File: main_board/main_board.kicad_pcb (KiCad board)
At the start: 2 copper layers, 160 x 110 mm, 154 parts, among them IC1 MP2722GRH-0000-Z, IC2 MP3429GL-Z, IC3 NX3DV42GU, IC4 TS921ID, IC5 CY7C65632-28LTXC, IC6 TS921ID, J1 USB3_A, J10 Conn_01x22_Female, J2 USB3_A, J22 690-019-298-412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

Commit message: Rev 1 draft
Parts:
- removed C18, C9: 100n, Capacitor_SMD:C_0805_2012Metric_Pad1.18x1.45mm_HandSolder
- removed H1, H2, H3, H4, H5, H6, H7, H8: MountingHole, CM5IO:MountingHole_2.7mm_M2.5_DIN965
- removed IC3: NX3DV42GU, 000_custom:NX3DV42GU
- removed the JMP at (113.6, 41.8)
- removed the JMP at (42.5, 37.8)
- added C65: 1u, Capacitor_SMD:C_0805_2012Metric_Pad1.18x1.45mm_HandSolder, F.Cu at (44.8, 36.0)
- added C66: 1u, Capacitor_SMD:C_0805_2012Metric_Pad1.18x1.45mm_HandSolder, F.Cu at (40.5, 35.9)
- added C67: 1u, Capacitor_SMD:C_0805_2012Metric_Pad1.18x1.45mm_HandSolder, F.Cu at (53.8, 31.8)
- added J11: 501568-0607-TR325, 000_custom:CONN_501568-0607-TR325_MOL, F.Cu at (117.6, 76.5)
- added J12: SM04B-XSRS-ETBLFSN, 000_custom:CONN_SM04B-XSRS-ETB_JST, F.Cu at (55.8, 46.7)
- added J13: SM10B-XSRS-ETB, 000_custom:CONN_SM10B-XSRS-ETB_JST, F.Cu at (50.1, 61.4)
- added MOSFET1: STL9P3LLH6, 000_custom:POWERFLAT_3P3X3P3_STM, F.Cu at (52.6, 38.5)
- added U8: STUSB4500QTR, 000_custom:STUSB4500, F.Cu at (42.9, 39.9)
- C1: footprint Capacitor_SMD:C_0805_2012Metric -> Capacitor_SMD:C_0805_2012Metric_Pad1.18x1.45mm_HandSolder
- R23: value 2.2K 1% -> 1K
- R5: value 0R -> 100K
- R9: value 2.2K 1% -> 10K
- moved R23 70.3 mm to (47.8, 37.7), turned to -90 degrees
- moved C15 67.3 mm to (49.0, 125.9), turned to -90 degrees
- moved C14 64.0 mm to (51.0, 125.9), turned to -90 degrees
- moved C4 63.5 mm to (70.8, 126.7), turned to 0 degrees
- moved L1 61.9 mm to (58.8, 124.2)
- moved C6 61.5 mm to (62.9, 125.6)
- moved R3 61.5 mm to (64.9, 125.7)
- moved R4 61.5 mm to (66.9, 125.7)
- moved U1 61.5 mm to (63.3, 122.4)
- moved C1 60.8 mm to (70.8, 124.7), turned to 0 degrees
- moved C10 60.8 mm to (52.8, 125.9), turned to -90 degrees
- moved C5 58.0 mm to (70.8, 122.8), turned to 0 degrees
- moved C11 57.6 mm to (54.7, 125.9), turned to -90 degrees
- moved J2 36.3 mm to (180.7, 110.0)
- moved J6 33.4 mm to (182.4, 76.3)
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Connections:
- C19 pad 1: /Battery management/VIN -> Net-(IC1-IN)
- IC1 pad 1: /Battery management/CC1 -> unconnected-(IC1-CC1-Pad1)
- IC1 pad 2: /Battery management/VIN -> Net-(IC1-IN)
- IC1 pad 20: /Battery management/USBC_MX2_USB2_N -> unconnected-(IC1-D--Pad20)
- IC1 pad 21: /Battery management/USBC_MX2_USB2_P -> unconnected-(IC1-D+-Pad21)
- IC1 pad 22: /Battery management/CC2 -> unconnected-(IC1-CC2_1-Pad22)
- IC1 pad 8: /Battery management/PMIC INTERRUPT -> unconnected-(IC1-~{INT}-Pad8)
- J10 pad 11: /CM5_HighSpeed/DPHY0_D2_N -> /CM5_HighSpeed/DPHY0_D1_P
- J10 pad 12: /CM5_HighSpeed/DPHY0_D2_P -> /CM5_HighSpeed/DPHY0_D1_N
- J10 pad 14: /CM5_HighSpeed/DPHY0_D3_N -> /CM5_HighSpeed/DPHY0_D0_P
- J10 pad 15: /CM5_HighSpeed/DPHY0_D3_P -> /CM5_HighSpeed/DPHY0_D0_N
- J10 pad 17: Net-(J10-Pin_17) -> /CM5_GPIO/+3.3v
- J10 pad 18: unconnected-(J10-Pin_18-Pad18) -> /CM5_GPIO/DPHY1_SDA
- J10 pad 19: GND -> /CM5_GPIO/DPHY1_SCL
- J10 pad 2: /CM5_HighSpeed/DPHY0_D0_N -> /CM5_HighSpeed/DPHY0_D3_P
- J10 pad 20: /CM5_GPIO/DPHY1_SDA -> /Battery management/+5V
- J10 pad 21: /CM5_GPIO/DPHY1_SCL -> /Battery management/+5V
- J10 pad 22: /CM5_GPIO/+3.3v -> /Battery management/+5V
- J10 pad 3: /CM5_HighSpeed/DPHY0_D0_P -> /CM5_HighSpeed/DPHY0_D3_N
- J10 pad 5: /CM5_HighSpeed/DPHY0_D1_N -> /CM5_HighSpeed/DPHY0_D2_P
- J10 pad 6: /CM5_HighSpeed/DPHY0_D1_P -> /CM5_HighSpeed/DPHY0_D2_N
- J10 pad 8: /CM5_HighSpeed/DPHY0_C_N -> /CM5_HighSpeed/DPHY0_C_P
- J10 pad 9: /CM5_HighSpeed/DPHY0_C_P -> /CM5_HighSpeed/DPHY0_C_N
- J2 pad 2: Net-(IC5-DD-[3]) -> Net-(IC5-DD-[1])
- J2 pad 3: Net-(IC5-DD+[3]) -> Net-(IC5-DD+[1])
- J5 pad A4: /Battery management/VIN -> Net-(U8-VDD)
- J5 pad A5: /Battery management/CC1 -> Net-(J5-CC1)
- J5 pad A6: /Battery management/USB2_P -> unconnected-(J5-D+-PadA6)
- J5 pad A7: /Battery management/USB2_N -> unconnected-(J5-D--PadA7)
- J5 pad B4: /Battery management/VIN -> Net-(U8-VDD)
- J5 pad B5: /Battery management/CC2 -> Net-(J5-CC2)
- J5 pad B6: /Battery management/USB2_P -> unconnected-(J5-D+-PadB6)
- J5 pad B7: /Battery management/USB2_N -> unconnected-(J5-D--PadB7)
- J6 pad 2: Net-(IC5-DD+[1]) -> Net-(IC5-DD+[3])
- J6 pad 3: Net-(IC5-DD-[1]) -> Net-(IC5-DD-[3])
- Module1 pad 103: /Battery management/USBC_MX1_USB2_N -> Net-(Module1B-USB2_N)
- Module1 pad 105: /Battery management/USBC_MX1_USB2_P -> Net-(Module1B-USB2_P)
- R12 pad 1: Net-(U6-ILIM) -> GND
- R12 pad 2: GND -> Net-(U6-ILIM)
- R23 pad 1: /CM5_GPIO/+3.3v -> Net-(U8-VDD)
- R23 pad 2: Net-(J10-Pin_17) -> Net-(U8-VBUS_VS_DISCH)
- R5 pad 1: /Battery management/USB2_N -> Net-(U8-VDD)
- R5 pad 2: /Battery management/USB2_N -> Net-(MOSFET1-G)
- R9 pad 1: /Battery management/VIN -> Net-(MOSFET1-G)
- R9 pad 2: GND -> Net-(U8-VBUS_EN_SNK)
- U3 pad 28: /Battery management/PMIC INTERRUPT -> unconnected-(U3-PB4-Pad28)
- U3 pad 29: /Battery management/OTG_SW -> unconnected-(U3-PB5-Pad29)
- U3 pad 30: /Battery management/USB_SW_VCC -> unconnected-(U3-PB6-Pad30)
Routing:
- net /Battery management/IIC_SDA: track 88.3 -> 236.1 mm, vias 2 -> 3
- net /Battery management/IIC_SCL: track 96.0 -> 217.2 mm, vias 2 -> 4
- net GND: track 412.5 -> 316.6 mm, vias 14 -> 16
- net /Battery management/+5V: track 637.5 -> 712.2 mm, vias 0 -> 4
- net Net-(Module1B-USB2_N): track 0.00 -> 68.0 mm
- net Net-(Module1B-USB2_P): track 0.00 -> 67.1 mm
- net /Battery management/USBC_MX1_USB2_N: track 62.4 -> 0.00 mm, vias 2 -> 0
- net /Battery management/USBC_MX1_USB2_P: track 58.8 -> 0.00 mm, vias 2 -> 0
- net /Battery management/USBC_MX2_USB2_N: track 49.2 -> 0.00 mm
- net /PCIe-M2/M2_3v3: track 120.1 -> 71.6 mm
- net /Battery management/USBC_MX2_USB2_P: track 47.4 -> 0.00 mm
- net Net-(U8-VDD): track 0.00 -> 43.2 mm
- net /CM5_HighSpeed/HDMI1_HOTPLUG: track 0.00 -> 42.7 mm
- net /CM5_HighSpeed/HDMI1_SDA: track 0.00 -> 42.4 mm
- net /CM5_HighSpeed/HDMI1_SCL: track 0.00 -> 42.1 mm
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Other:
- board text added: "Rev 1"
- board text added: "Shop: - Jack - Molex - Power stuff - Passives - M.2 screws"
- board text removed: "TODO: - Cleanup diff pairs - LCD (HDMI1)"

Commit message: Cleanup silks
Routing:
- net GND: track 316.6 -> 320.6 mm
- net /Battery management/+5V: track 712.2 -> 708.9 mm
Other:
- board text added: "PMIC USB, prog/debug only"
- board text added: "TODO: - Ensure conns are at correct positions"
- board text added: "Warning! Not a standard RPI header!"

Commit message: Final fixes
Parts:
- moved C6 3.06 mm to (66.0, 125.3)
- moved U1 3.06 mm to (66.4, 122.1)
- moved C4 3.06 mm to (73.9, 126.4)
- moved R3 3.06 mm to (68.0, 125.3)
- moved R4 3.06 mm to (70.0, 125.3)
- moved C1 3.06 mm to (73.9, 124.4)
- moved C5 3.06 mm to (73.9, 122.5)
- moved C10 2.51 mm to (54.2, 123.8)
- moved C11 2.51 mm to (56.1, 123.8)
- moved C15 2.51 mm to (50.4, 123.8)
- moved C14 2.51 mm to (52.3, 123.8)
- moved L1 2.01 mm to (60.7, 123.7), turned to 180 degrees
- moved J6 0.71 mm to (181.7, 76.3)
- moved J7 0.70 mm to (181.7, 92.4)
- moved C16 0.20 mm to (49.2, 91.2)
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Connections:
- U3 pad 20: unconnected-(U3-PD2-Pad20) -> GND
- U3 pad 21: unconnected-(U3-PD3-Pad21) -> GND
- U3 pad 22: unconnected-(U3-PD5-Pad22) -> GND
- U3 pad 36: unconnected-(U3-PF7-Pad36) -> GND
- U3 pad 37: unconnected-(U3-PF6-Pad37) -> GND
- U3 pad 38: unconnected-(U3-PF5-Pad38) -> GND
- U3 pad 39: unconnected-(U3-PF4-Pad39) -> GND
- U3 pad 40: unconnected-(U3-PF1-Pad40) -> GND
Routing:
- net /Battery management/+5V: track 708.9 -> 698.5 mm
- net /Battery management/PMIC_3.3V: track 52.9 -> 60.7 mm, vias 3 -> 2
- net GND: track 320.6 -> 326.5 mm
- net /PCIe-M2/M2_3v3: track 71.6 -> 77.3 mm
- net /CM5_HighSpeed/PCIE_PWR_EN: track 57.7 -> 62.9 mm
- net Net-(IC5-DD+[3]): track 22.5 -> 23.1 mm
- net Net-(IC5-DD-[2]): track 20.3 -> 19.7 mm
- net Net-(IC5-DD+[2]): track 18.8 -> 18.2 mm

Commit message: Fix fried USB hub
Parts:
- added H1: MountingHole, CM5IO:MountingHole_2.7mm_M2.5_DIN965, F.Cu at (-35.3, 21.9)
- added H2: MountingHole, CM5IO:MountingHole_2.7mm_M2.5_DIN965, F.Cu at (-35.3, 28.1)
- added H3: MountingHole, CM5IO:MountingHole_2.7mm_M2.5_DIN965, F.Cu at (-29.1, 21.9)
- added H4: MountingHole, CM5IO:MountingHole_2.7mm_M2.5_DIN965, F.Cu at (-29.1, 28.1)
- added H5: MountingHole, CM5IO:MountingHole_2.7mm_M2.5_DIN965, F.Cu at (-22.8, 21.9)
- added H6: MountingHole, CM5IO:MountingHole_2.7mm_M2.5_DIN965, F.Cu at (-22.8, 28.1)
- added H7: MountingHole, CM5IO:MountingHole_2.7mm_M2.5_DIN965, F.Cu at (-16.6, 21.9)
- added H8: MountingHole, CM5IO:MountingHole_2.7mm_M2.5_DIN965, F.Cu at (-16.6, 28.1)
- added JMP: R_0805_2012Metric_Pad1.20x1.40mm_HandSolder, Resistor_SMD:R_0805_2012Metric_Pad1.20x1.40mm_HandSolder, F.Cu at (153.2, 85.5)
- added JMP: 0.01R, Resistor_SMD:R_1206_3216Metric_Pad1.30x1.75mm_HandSolder, F.Cu at (158.8, 86.8)
- added R44: 100k, Resistor_SMD:R_0805_2012Metric_Pad1.20x1.40mm_HandSolder, F.Cu at (154.1, 76.9)
- MOSFET1: footprint 000_custom:POWERFLAT_3P3X3P3_STM -> Package_SON:Diodes_PowerDI3333-8
- R10: value 47k -> 43K
- Y2: value Crystal -> 12MHz
- moved C45 2.13 mm to (160.6, 90.0)
- moved R20 1.65 mm to (154.1, 80.7)
- moved R21 1.65 mm to (154.1, 78.8)
- moved R22 1.65 mm to (154.1, 82.5)
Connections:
- C45 pad 1: Net-(IC5-VCC_A_1) -> Net-(IC5-SELFPWR)
- C47 pad 1: /USB hub/HUBVCC -> Net-(IC5-SELFPWR)
- IC5 pad 21: /USB hub/HUBVCC -> Net-(IC5-SELFPWR)
- IC5 pad 22: /USB hub/HUBVCC -> Net-(IC5-SELFPWR)
- IC5 pad 23: /USB hub/HUBVCC -> Net-(IC5-GANG)
- IC5 pad 28: /USB hub/VBUS -> Net-(IC5-SELFPWR)
- IC5 pad 5: Net-(IC5-VCC_A_1) -> Net-(IC5-SELFPWR)
- R18 pad 1: /USB hub/HUBVCC -> Net-(IC5-SELFPWR)
- R19 pad 1: /USB hub/HUBVCC -> Net-(IC5-SELFPWR)
- R20 pad 1: /USB hub/HUBVCC -> Net-(IC5-SELFPWR)
- R21 pad 1: /USB hub/HUBVCC -> Net-(IC5-SELFPWR)
- R22 pad 1: /USB hub/HUBVCC -> Net-(IC5-SELFPWR)
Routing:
- net Net-(IC5-SELFPWR): track 0.00 -> 36.1 mm
- net /USB hub/HUBVCC: track 18.5 -> 0.00 mm
- net Net-(IC5-GANG): track 0.00 -> 5.76 mm
- net Net-(IC5-VCC_A_1): track 2.65 -> 0.00 mm
- net /USB hub/VBUS: track 147.9 -> 149.9 mm
- net Net-(IC5-OVR_#_[1]): track 4.91 -> 3.13 mm
- net Net-(IC5-OVR_#_[2]): track 6.00 -> 4.52 mm
- net Net-(IC5-PWR#/_I2C_SDA): track 3.21 -> 2.68 mm
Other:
- board text removed: "Shop: - Jack - Molex - Power stuff - Passives - M.2 screws"
- board text removed: "TODO: - Ensure conns are at correct positions"

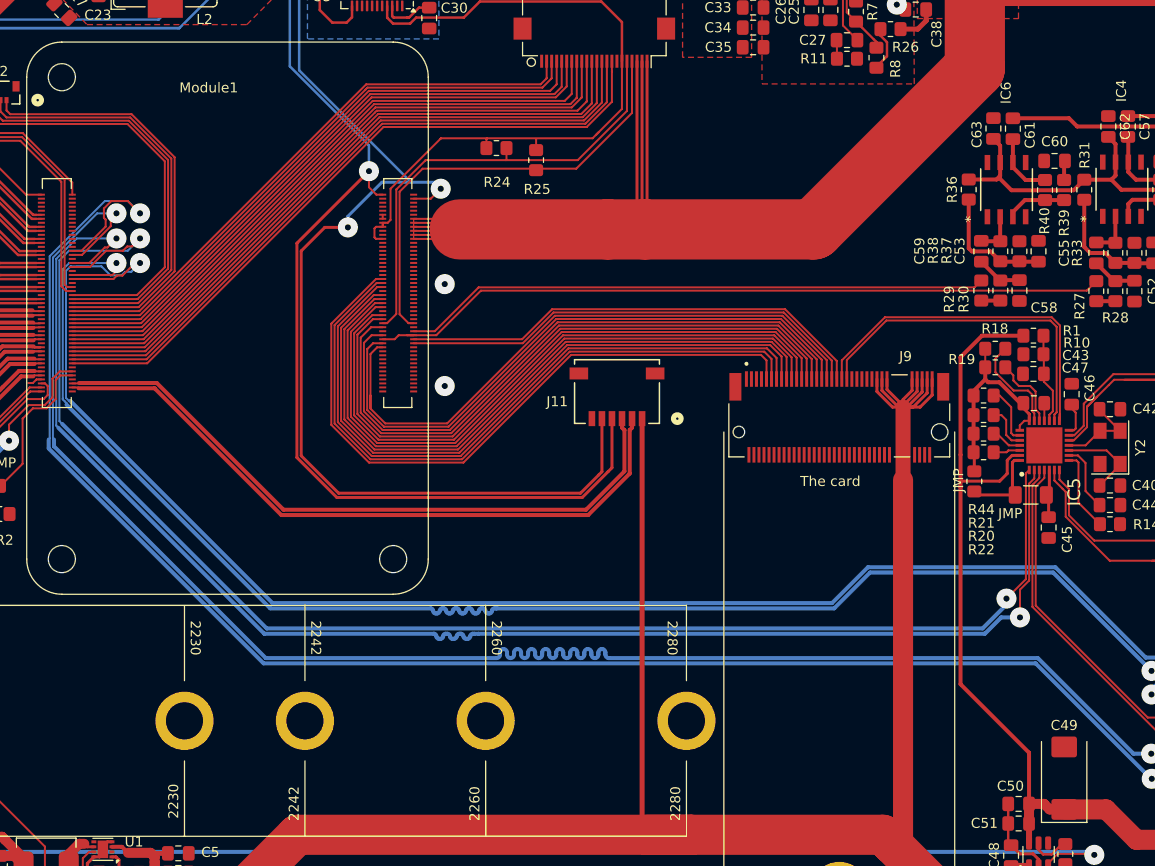
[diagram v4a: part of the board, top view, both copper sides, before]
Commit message: Fix frying usb hub again
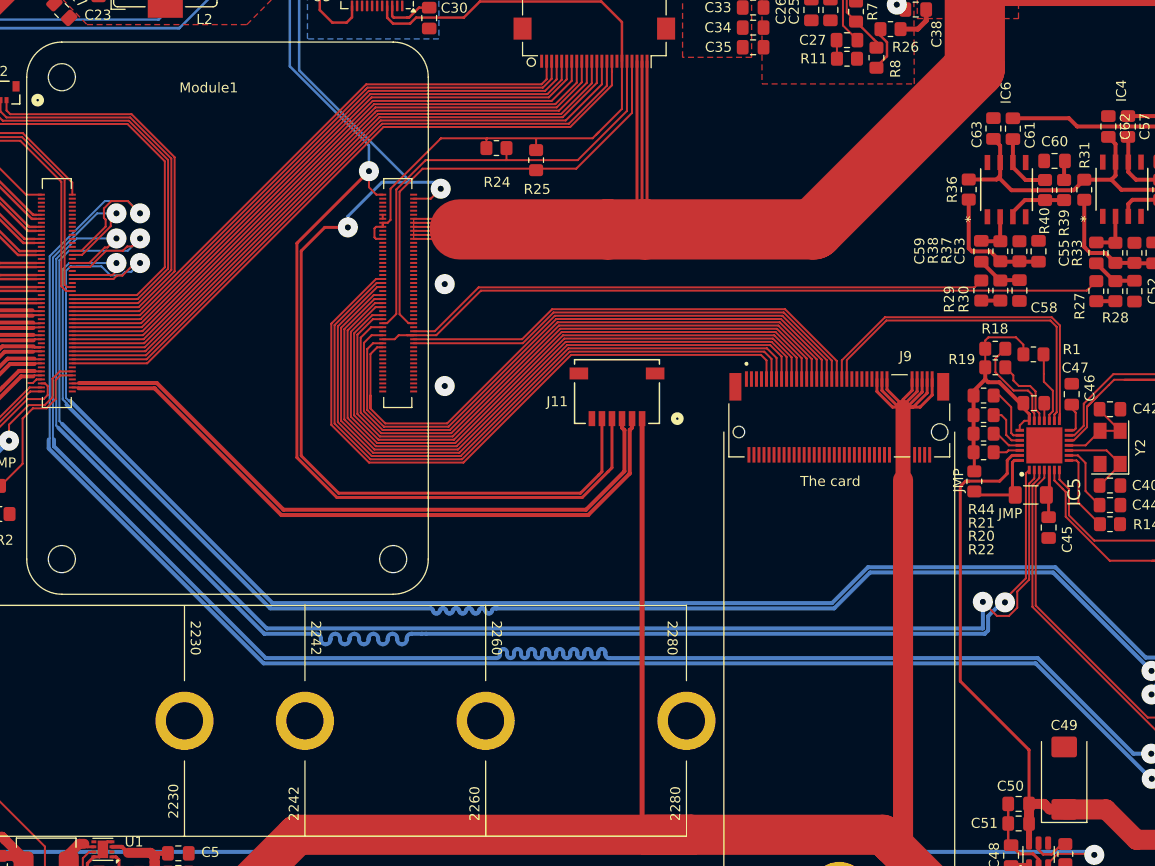
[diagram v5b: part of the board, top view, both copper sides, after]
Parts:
- removed C43: 1u, Capacitor_SMD:C_0805_2012Metric_Pad1.18x1.45mm_HandSolder
- removed R10: 43K, Resistor_SMD:R_0805_2012Metric_Pad1.20x1.40mm_HandSolder
- R1: value 1k -> 10k
- moved R1 1.86 mm to (159.0, 72.8)
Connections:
- C44 pad 1: Net-(IC5-VCC_A_2) -> Net-(IC5-SELFPWR)
- IC5 pad 1: /CM5_HighSpeed/USB3_1_DP -> /CM5_HighSpeed/USB3_1_DN
- IC5 pad 2: /CM5_HighSpeed/USB3_1_DN -> /CM5_HighSpeed/USB3_1_DP
- IC5 pad 9: Net-(IC5-VCC_A_2) -> Net-(IC5-SELFPWR)
- R1 pad 2: /USB hub/VBUS -> Net-(IC5-SELFPWR)
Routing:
- net /USB hub/VBUS: track 149.9 -> 129.5 mm
- net Net-(IC5-SELFPWR): track 36.1 -> 48.9 mm
- net Net-(IC5-VCC_A_2): track 6.74 -> 0.00 mm
- net /CM5_HighSpeed/USB3_1_DP: track 151.1 -> 154.8 mm
- net /CM5_HighSpeed/USB3_1_DN: track 151.0 -> 154.3 mm
- net GND: track 326.5 -> 323.3 mm
- net Net-(IC5-RESET#): track 9.01 -> 7.16 mm
- net /CM5_HighSpeed/DPHY0_D1_P: track 66.0 -> 64.8 mm
- net /CM5_HighSpeed/DPHY0_D1_N: track 66.7 -> 65.5 mm
- net /CM5_HighSpeed/DPHY0_D0_P: track 67.9 -> 67.0 mm
- net /CM5_HighSpeed/DPHY0_D0_N: track 68.6 -> 67.6 mm
- net /CM5_HighSpeed/DPHY0_C_P: track 63.7 -> 62.8 mm
- net /CM5_HighSpeed/DPHY0_C_N: track 64.3 -> 63.4 mm

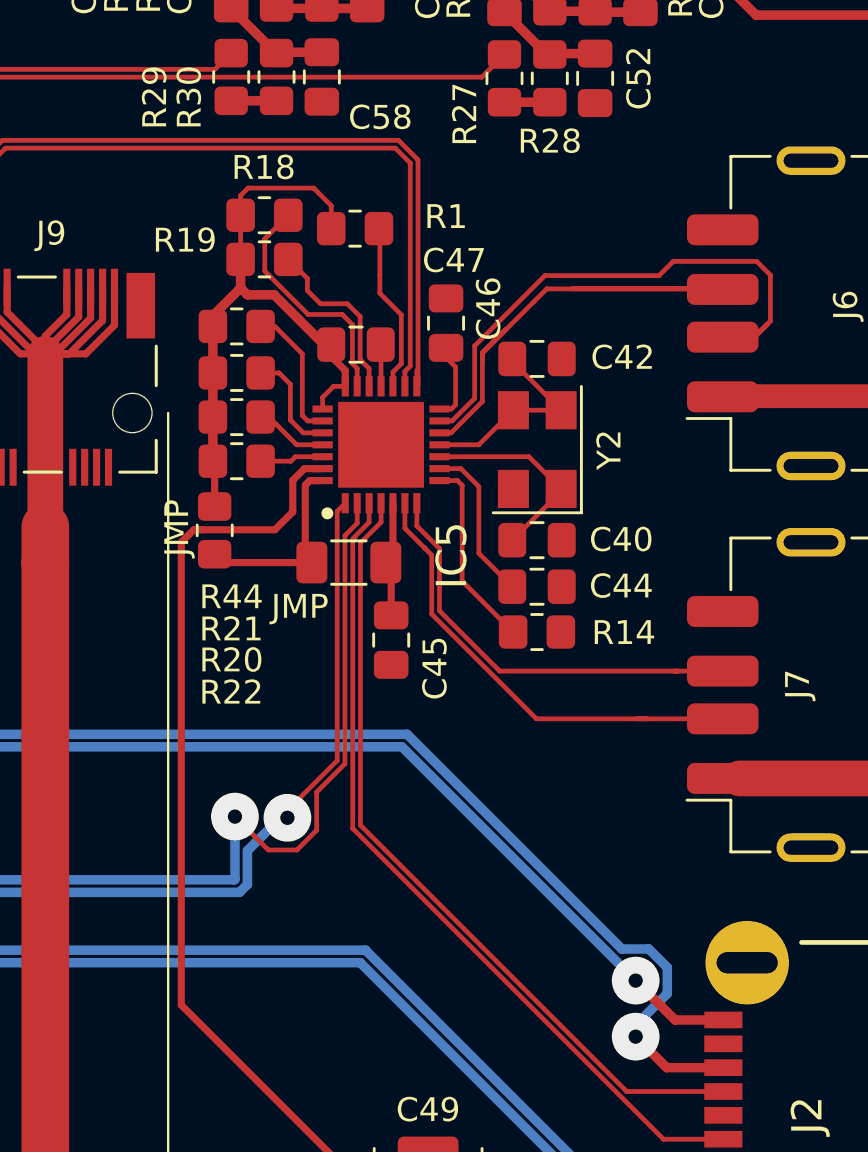
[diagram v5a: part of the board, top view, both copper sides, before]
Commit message: Remove passives from hub
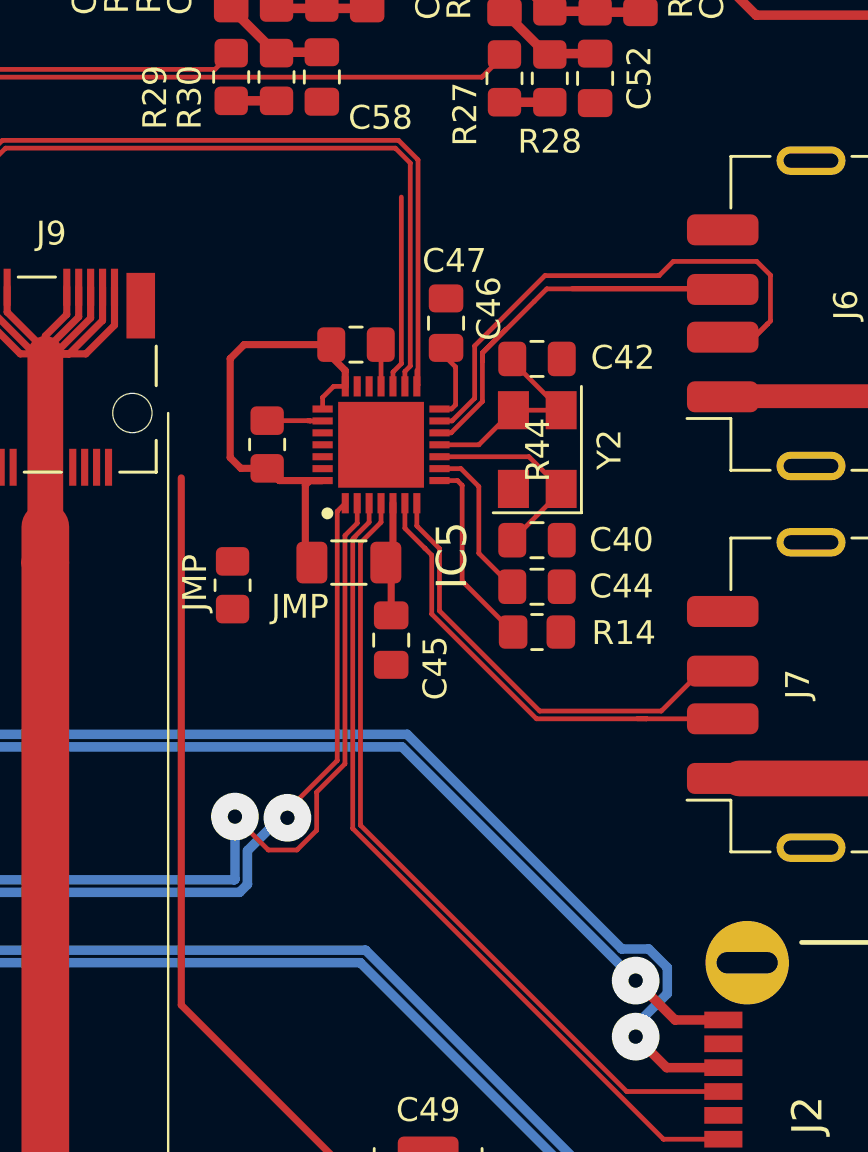
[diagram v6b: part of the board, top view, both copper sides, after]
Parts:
- removed R1, R18, R19, R20, R21: 10k, Resistor_SMD:R_0805_2012Metric_Pad1.20x1.40mm_HandSolder
- removed R22: 100k, Resistor_SMD:R_0805_2012Metric_Pad1.20x1.40mm_HandSolder
- moved R44 5.11 mm to (155.3, 81.8), turned to 90 degrees
- moved JMP 2.42 mm to (153.9, 87.8)
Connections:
- C44 pad 1: Net-(IC5-SELFPWR) -> /USB hub/HUB3V3
- C45 pad 1: Net-(IC5-SELFPWR) -> /USB hub/HUB3V3
- C47 pad 1: Net-(IC5-SELFPWR) -> /USB hub/HUB3V3
- IC5 pad 17: Net-(IC5-RESET#) -> /USB hub/HUB3V3
- IC5 pad 19: Net-(IC5-OVR_#_[4]) -> unconnected-(IC5-OVR_#_[4]-Pad19)
- IC5 pad 20: Net-(IC5-OVR_#_[3]) -> unconnected-(IC5-OVR_#_[3]-Pad20)
- IC5 pad 21: Net-(IC5-SELFPWR) -> /USB hub/HUB3V3
- IC5 pad 22: Net-(IC5-SELFPWR) -> /USB hub/HUB3V3
- IC5 pad 24: Net-(IC5-OVR_#_[2]) -> unconnected-(IC5-OVR_#_[2]-Pad24)
- IC5 pad 25: Net-(IC5-OVR_#_[1]) -> unconnected-(IC5-OVR_#_[1]-Pad25)
- IC5 pad 26: Net-(IC5-PWR#/_I2C_SDA) -> unconnected-(IC5-PWR#/_I2C_SDA-Pad26)
- IC5 pad 28: Net-(IC5-SELFPWR) -> /USB hub/HUB3V3
- IC5 pad 5: Net-(IC5-SELFPWR) -> /USB hub/HUB3V3
- IC5 pad 9: Net-(IC5-SELFPWR) -> /USB hub/HUB3V3
- JMP pad 1: Net-(IC5-SELFPWR) -> /USB hub/HUB3V3 (x2)
- JMP pad 2: Net-(IC5-SELFPWR) -> /USB hub/HUB3V3
- R44 pad 1: Net-(IC5-SELFPWR) -> /USB hub/HUB3V3
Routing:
- net Net-(IC5-SELFPWR): track 48.9 -> 6.58 mm
- net /USB hub/HUB3V3: track 0.00 -> 35.5 mm
- net Net-(IC5-OVR_#_[3]): track 10.0 -> 0.00 mm
- net Net-(IC5-OVR_#_[4]): track 7.39 -> 0.00 mm
- net Net-(IC5-RESET#): track 7.16 -> 0.00 mm
- net /USB hub/VBUS: track 129.5 -> 124.2 mm
- net Net-(IC5-OVR_#_[2]): track 4.52 -> 0.00 mm
- net Net-(IC5-GANG): track 5.76 -> 2.43 mm
- net Net-(IC5-OVR_#_[1]): track 3.13 -> 0.00 mm
- net Net-(IC5-PWR#/_I2C_SDA): track 2.68 -> 0.00 mm
- net Net-(IC5-DD+[2]): track 18.0 -> 19.2 mm
